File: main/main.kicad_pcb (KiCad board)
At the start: 2 copper layers, 39.2 x 36.2 mm, 90 parts, among them IC1 STM32U073CCU6, IC2 IC_TEXAS_TPS62743YFPR, IC3 IC_TEXAS_TPS62743YFPR, IC4 PAM8302AASCR, J3 USB_C_Receptacle_USB2.0_16P, J4 SM03B-SRSS-TB, Q1 DMG1012T-7, SW1 PTS810 SJK 250 SMTR LFS, U1 RP2350_60QFN, U2 IC_ESPIF_ESP32-C3-MINI-1-N4, U3 W25Q32RVXHJQ TR, U4 TMF8806, U6 450mA 4.2V, X1 XTAL_ABRACON_ABS07-32.768KHZ-T, Y1 ECS-120-8-33-JGN-TR

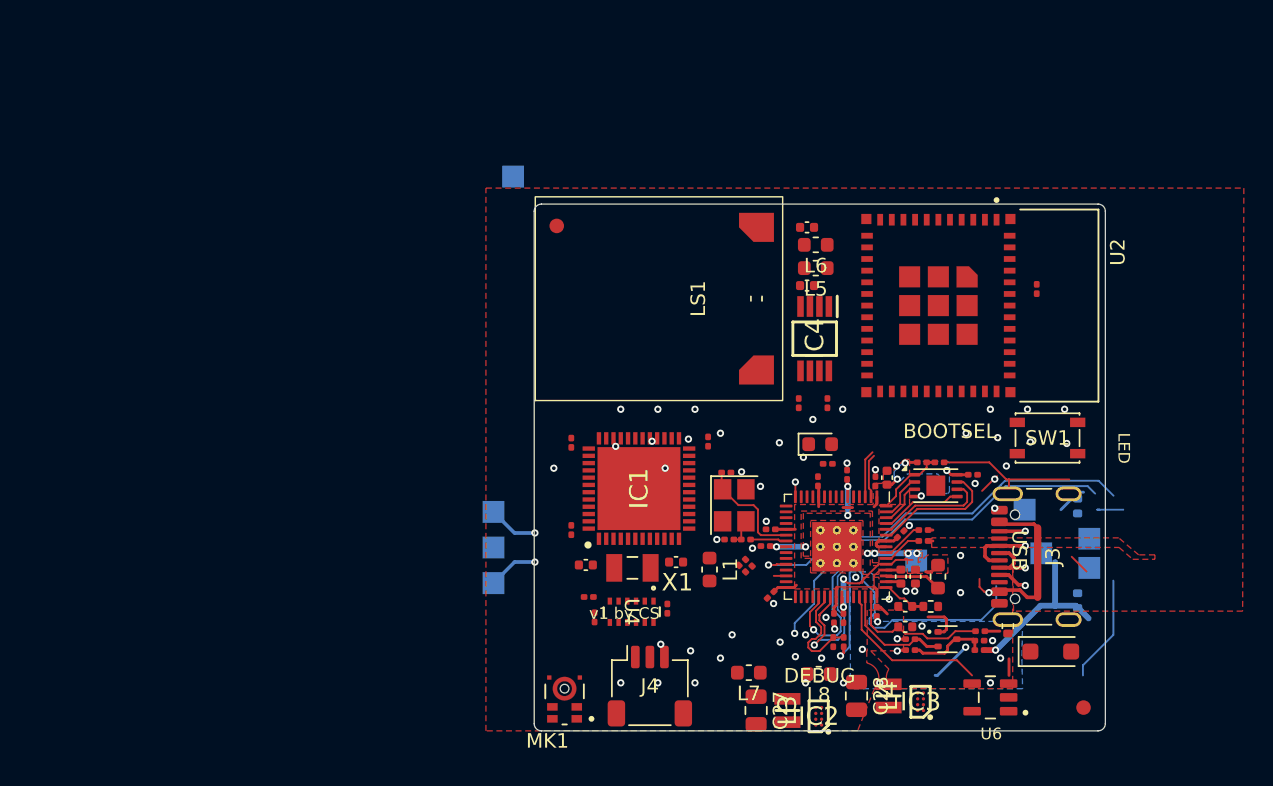
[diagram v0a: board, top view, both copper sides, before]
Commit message: last commit with pi-pico still on
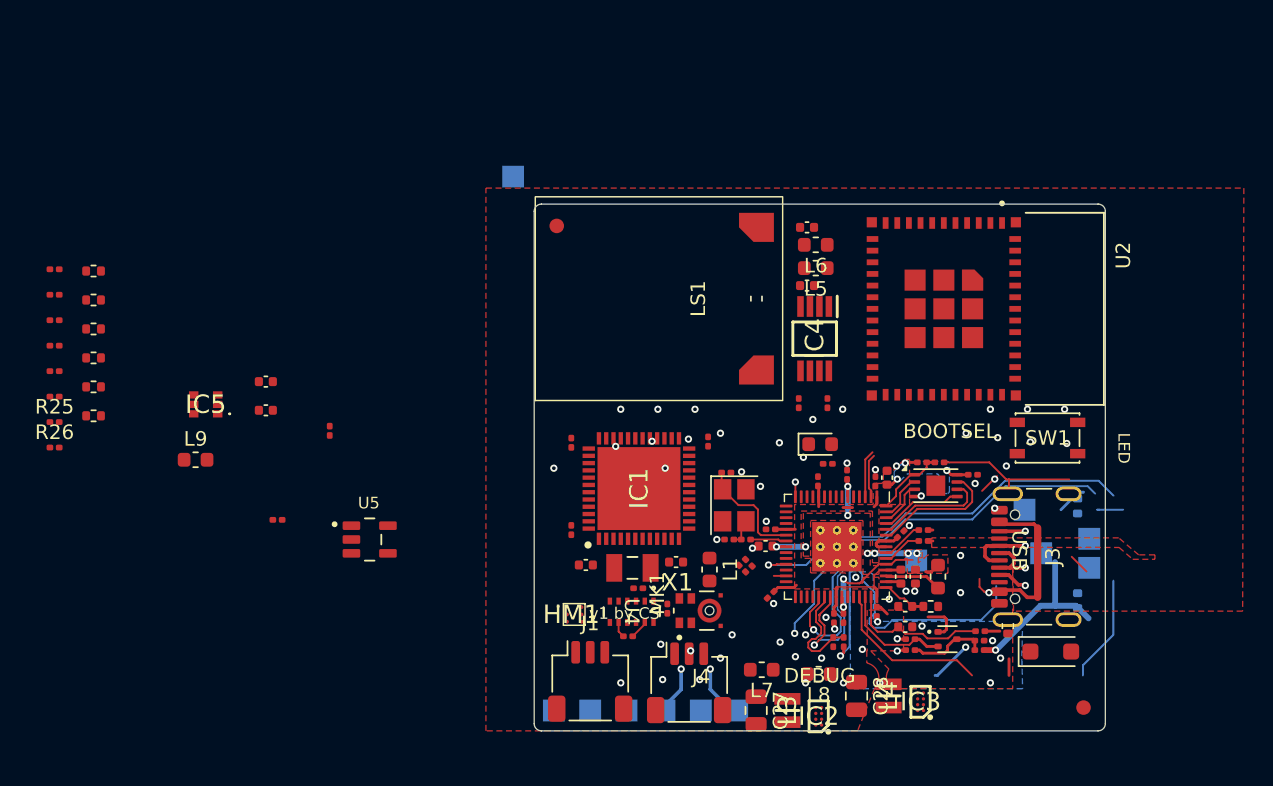
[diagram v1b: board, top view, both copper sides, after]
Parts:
- removed U6: 450mA 4.2V, smv_footprints:SOT95P280X145-5N
- added C35: 100NF_0201_10V_X7R, smv_footprints:C_0201_0603Metric, F.Cu at (111.6, 102.7)
- added C36: 100NF_0201_10V_X7R, smv_footprints:C_0201_0603Metric, F.Cu at (96.3, 85.5)
- added C37: 100NF_0201_10V_X7R, smv_footprints:C_0201_0603Metric, F.Cu at (96.3, 87.2)
- added C38: 100NF_0201_10V_X7R, smv_footprints:C_0201_0603Metric, F.Cu at (96.3, 89.0)
- added C39: 100NF_0201_10V_X7R, smv_footprints:C_0201_0603Metric, F.Cu at (96.3, 90.7)
- added C40: 100NF_0201_10V_X7R, smv_footprints:C_0201_0603Metric, F.Cu at (96.3, 92.5)
- added C41: 100NF_0201_10V_X7R, smv_footprints:C_0201_0603Metric, F.Cu at (96.3, 94.2)
- added C42: 4.7UF 0402 10V X7R, smv_footprints:C_0402_1005Metric, F.Cu at (110.8, 93.2)
- added C43: 4.7UF 0402 10V X7R, smv_footprints:C_0402_1005Metric, F.Cu at (110.8, 95.2)
- added HM1: HDC2010YPAR, smv_footprints:IC_TEXAS_HDC2010YPAR, F.Cu at (132.0, 109.2)
- added IC5: DIOD_PHOTO_VISHAY_VEML6035, smv_footprints:DIOD_PHOTO_VISHAY_VEML6035, F.Cu at (106.7, 94.8)
- added J1: SM03B-SRSS-TB, Connector_JST:JST_SH_SM03B-SRSS-TB_1x03-1MP_P1.00mm_Horizontal, F.Cu at (133.1, 113.8)
- added L9: INDC_BEAD_BLM18AG601SN1D, Inductor_SMD:L_0603_1608Metric, F.Cu at (106.0, 98.6)
- added R15: 10K 0402, smv_footprints:R_0402_1005Metric, F.Cu at (99.0, 89.6)
- added R2: 10K 0402, smv_footprints:R_0402_1005Metric, F.Cu at (99.0, 85.6)
- added R22: 10K 0402, smv_footprints:R_0402_1005Metric, F.Cu at (99.0, 91.6)
- added R23: 10K 0402, smv_footprints:R_0402_1005Metric, F.Cu at (99.0, 93.6)
- added R24: 10K 0402, smv_footprints:R_0402_1005Metric, F.Cu at (99.0, 95.5)
- added R25: 100R, Resistor_SMD:R_0201_0603Metric, F.Cu at (96.3, 96.0)
- added R26: 100R, Resistor_SMD:R_0201_0603Metric, F.Cu at (96.3, 97.7)
- added R8: 10K 0402, smv_footprints:R_0402_1005Metric, F.Cu at (99.0, 87.6)
- added TP11: TestPoint, TestPoint:TestPoint_Pad_1.5x1.5mm, B.Cu at (133.1, 115.8)
- added TP12: TestPoint, TestPoint:TestPoint_Pad_1.5x1.5mm, B.Cu at (135.6, 115.8)
- added TP4: TestPoint, TestPoint:TestPoint_Pad_1.5x1.5mm, B.Cu at (130.6, 115.8)
- added U5: 450mA 4.2V, smv_footprints:SOT95P280X145-5N, F.Cu at (117.9, 104.0)
- C13, C18, C19, C20, C21: value 4u7 -> 4.7UF 0402 10V X7R; footprint Capacitor_SMD:C_0402_1005Metric -> smv_footprints:C_0402_1005Metric
- C9: value 4u7 -> 4.7UF 0402 10V X7R; footprint Capacitor_SMD:C_0201_0603Metric -> smv_footprints:C_0402_1005Metric
- moved C32 49.6 mm to (115.2, 96.6)
- moved TP10 18.9 mm to (143.2, 115.8), turned to -90 degrees
- moved TP9 18.1 mm to (140.7, 115.8), turned to -90 degrees
- moved TP8 18.0 mm to (138.2, 115.8), turned to -90 degrees
- moved MK1 11.1 mm to (140.6, 108.9), turned to 90 degrees
- moved C33 3.45 mm to (136.4, 107.4), turned to 0 degrees
- moved J4 2.71 mm to (139.9, 113.9)
- moved C34 2.64 mm to (135.7, 110.7), turned to 0 degrees
- moved L7 0.91 mm to (144.9, 113.0)
- moved U2 0.44 mm to (160.1, 88.2)
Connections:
- net Net-(IC1-PA4) renamed /Low Power/AUDIO_OUT
- C10 pad 2: unconnected-(C10-Pad2) -> GND
- C19 pad 1: +1V1 -> unconnected-(C19-Pad1)
- C19 pad 2: GND -> unconnected-(C19-Pad2)
- C20 pad 2: GND -> unconnected-(C20-Pad2)
- C26 pad 1: Net-(IC1-VDDUSB) -> +1V8
- C27 pad 1: Net-(IC2-VOS) -> +1V8
- C31 pad 1: Net-(U4-VDDC) -> +3V3
- C32 pad 1: unconnected-(C32-Pad1) -> +1V8
- C32 pad 2: unconnected-(C32-Pad2) -> GND
- C33 pad 1: Net-(U4-GND) -> +3V3
- C33 pad 2: Net-(U4-VDD) -> GND
- C34 pad 1: Net-(U4-VDDV) -> +3V3
- C34 pad 2: Net-(U4-GNDV) -> GND
- C6 pad 2: unconnected-(C6-Pad2) -> GND
- C9 pad 2: GND -> unconnected-(C9-Pad2)
- IC1 pad 1: unconnected-(IC1-VBAT-Pad1) -> +1V8
- IC1 pad 19: unconnected-(IC1-PB1-Pad19) -> Net-(IC1-PB1)
- IC1 pad 23: unconnected-(IC1-VSS_1-Pad23) -> GND
- IC1 pad 25: unconnected-(IC1-PB12-Pad25) -> /Low Power/3V3_EN
- IC1 pad 26: unconnected-(IC1-PB13-Pad26) -> Net-(IC1-PB13)
- IC1 pad 27: unconnected-(IC1-PB14-Pad27) -> Net-(IC1-PB14)
- IC1 pad 28: unconnected-(IC1-PB15-Pad28) -> Net-(HM1-DRDY_/_INT)
- IC1 pad 34: unconnected-(IC1-PA13-Pad34) -> SD_ST
- IC1 pad 35: unconnected-(IC1-VSS_2-Pad35) -> GND
- IC1 pad 36: Net-(IC1-VDDUSB) -> +1V8
- IC1 pad 37: unconnected-(IC1-PA14-Pad37) -> SC_ST
- IC1 pad 38: unconnected-(IC1-PA15-Pad38) -> Net-(IC1-PA15)
- IC1 pad 39: unconnected-(IC1-PB3-Pad39) -> /Low Power/1V8_PP1
- IC1 pad 40: unconnected-(IC1-PB4-Pad40) -> /Low Power/1V8_PP2
- IC1 pad 41: unconnected-(IC1-PB5-Pad41) -> Net-(IC1-PB5)
- IC1 pad 42: unconnected-(IC1-PB6-Pad42) -> Net-(IC1-PB6)
- IC1 pad 43: unconnected-(IC1-PB7-Pad43) -> Net-(IC1-PB7)
- IC1 pad 45: unconnected-(IC1-PB8-Pad45) -> /Low Power/LIDAR_SCL
- IC1 pad 46: unconnected-(IC1-PB9-Pad46) -> /Low Power/LIDAR_SDA
- IC1 pad 47: unconnected-(IC1-VSS_3-Pad47) -> GND
- IC1 pad 49: unconnected-(IC1-EP-Pad49) -> GND
- IC2 pad A2: unconnected-(IC2-VIN-PadA2) -> Net-(IC2-EN)
- IC2 pad B1: unconnected-(IC2-EN-PadB1) -> Net-(IC2-EN)
- IC2 pad C1: unconnected-(IC2-VSEL1-PadC1) -> GND
- IC2 pad C2: Net-(IC2-VOS) -> +1V8
- IC2 pad D1: unconnected-(IC2-VSEL2-PadD1) -> Net-(IC2-EN)
- IC2 pad D2: unconnected-(IC2-VSEL3-PadD2) -> GND
- IC3 pad A2: unconnected-(IC3-VIN-PadA2) -> Net-(IC3-VIN)
- IC3 pad B1: unconnected-(IC3-EN-PadB1) -> /Low Power/3V3_EN
- IC3 pad C1: unconnected-(IC3-VSEL1-PadC1) -> Net-(IC3-VIN)
- IC3 pad D1: unconnected-(IC3-VSEL2-PadD1) -> Net-(IC3-VIN)
- IC3 pad D2: unconnected-(IC3-VSEL3-PadD2) -> Net-(IC3-VIN)
- IC4 pad 1: unconnected-(IC4-~{SD}-Pad1) -> Net-(IC1-PB1)
- IC4 pad 6: unconnected-(IC4-VDD-Pad6) -> +BATT
- L1 pad 1: unconnected-(L1-Pad1) -> +1V8
- L3 pad 2: Net-(IC2-VOS) -> +1V8
- L7 pad 1: Net-(IC2-VOS) -> +BATT
- L7 pad 2: unconnected-(L7-Pad2) -> Net-(IC2-EN)
- L8 pad 2: unconnected-(L8-Pad2) -> +3V3
- MK1 pad 1: unconnected-(MK1-DATA-Pad1) -> Net-(IC1-PB14)
- MK1 pad 2: unconnected-(MK1-SELECT-Pad2) -> GND
- MK1 pad 3_1: unconnected-(MK1-GND-Pad3_1) -> GND
- MK1 pad 3_2: unconnected-(MK1-GND__1-Pad3_2) -> GND
- MK1 pad 6: unconnected-(MK1-CLK-Pad6) -> Net-(IC1-PB13)
- MK1 pad 7: unconnected-(MK1-VDD-Pad7) -> +1V8
- U2 pad 1: Net-(U2-GND-Pad1) -> GND
- U2 pad 11: Net-(U2-GND-Pad1) -> GND
- U2 pad 14: Net-(U2-GND-Pad1) -> GND
- U2 pad 2: Net-(U2-GND-Pad1) -> GND
- U2 pad 3: unconnected-(U2-3V3-Pad3) -> +3V3
- U2 pad 36: Net-(U2-GND-Pad1) -> GND
- U2 pad 37: Net-(U2-GND-Pad1) -> GND
- U2 pad 38: Net-(U2-GND-Pad1) -> GND
- U2 pad 39: Net-(U2-GND-Pad1) -> GND
- U2 pad 40: Net-(U2-GND-Pad1) -> GND
- U2 pad 41: Net-(U2-GND-Pad1) -> GND
- U2 pad 42: Net-(U2-GND-Pad1) -> GND
- U2 pad 43: Net-(U2-GND-Pad1) -> GND
- U2 pad 44: Net-(U2-GND-Pad1) -> GND
- U2 pad 45: Net-(U2-GND-Pad1) -> GND
- U2 pad 46: Net-(U2-GND-Pad1) -> GND
- U2 pad 47: Net-(U2-GND-Pad1) -> GND
- U2 pad 48: Net-(U2-GND-Pad1) -> GND
- U2 pad 49_1: Net-(U2-GND-Pad1) -> GND
- U2 pad 49_2: Net-(U2-GND-Pad1) -> GND
- U2 pad 49_3: Net-(U2-GND-Pad1) -> GND
- U2 pad 49_4: Net-(U2-GND-Pad1) -> GND
- U2 pad 49_5: Net-(U2-GND-Pad1) -> GND
- U2 pad 49_6: Net-(U2-GND-Pad1) -> GND
- U2 pad 49_7: Net-(U2-GND-Pad1) -> GND
- U2 pad 49_8: Net-(U2-GND-Pad1) -> GND
- U2 pad 49_9: Net-(U2-GND-Pad1) -> GND
- U2 pad 50: Net-(U2-GND-Pad1) -> GND
- U2 pad 51: Net-(U2-GND-Pad1) -> GND
- U2 pad 52: Net-(U2-GND-Pad1) -> GND
- U2 pad 53: Net-(U2-GND-Pad1) -> GND
- U4 pad 1: Net-(U4-VDDC) -> +3V3
- U4 pad 11: Net-(U4-GNDV) -> GND
- U4 pad 12: Net-(U4-VDDV) -> +3V3
- U4 pad 3: unconnected-(U4-GPIO0-Pad3) -> /Low Power/1V8_PP1
- U4 pad 4: unconnected-(U4-INT-Pad4) -> Net-(IC1-PA15)
- U4 pad 5: unconnected-(U4-SCL-Pad5) -> /Low Power/LIDAR_SCL
- U4 pad 6: unconnected-(U4-SDA-Pad6) -> /Low Power/LIDAR_SDA
- U4 pad 7: Net-(U4-VDD) -> GND
- U4 pad 8: Net-(U4-GND) -> +3V3
- U4 pad 9: unconnected-(U4-EN-Pad9) -> /Low Power/1V8_PP1
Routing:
- net GND: track 14.6 -> 16.3 mm, vias 49 -> 48
- net +3V3: track 23.5 -> 24.6 mm, vias 3 -> 4
- net unconnected-(C6-Pad2): track 0.38 -> 0.00 mm, vias 1 -> 0
- net unconnected-(U6-VBAT-Pad3): vias 1 -> 0
- net unconnected-(L8-Pad2): vias 1 -> 0
- net unconnected-(IC4-~{SD}-Pad1): vias 1 -> 0
- net unconnected-(IC1-PA8-Pad29): vias 0 -> 1
- net unconnected-(IC1-EP-Pad49): vias 1 -> 0
- net unconnected-(C9-Pad2): vias 0 -> 1
- net unconnected-(C19-Pad2): vias 0 -> 1
- net Net-(U2-GND-Pad1): vias 3 -> 0
- net Net-(IC1-PB1): vias 0 -> 1
- net (no net): vias 0 -> 4
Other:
- board text added: "PICO SWD GND SWC"
- board text added: "STM SWD GND SWC"
- board text removed: "CLK"
- board text removed: "DIO"
- board text removed: "GND"

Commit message: added leds and removed pico, changed outline
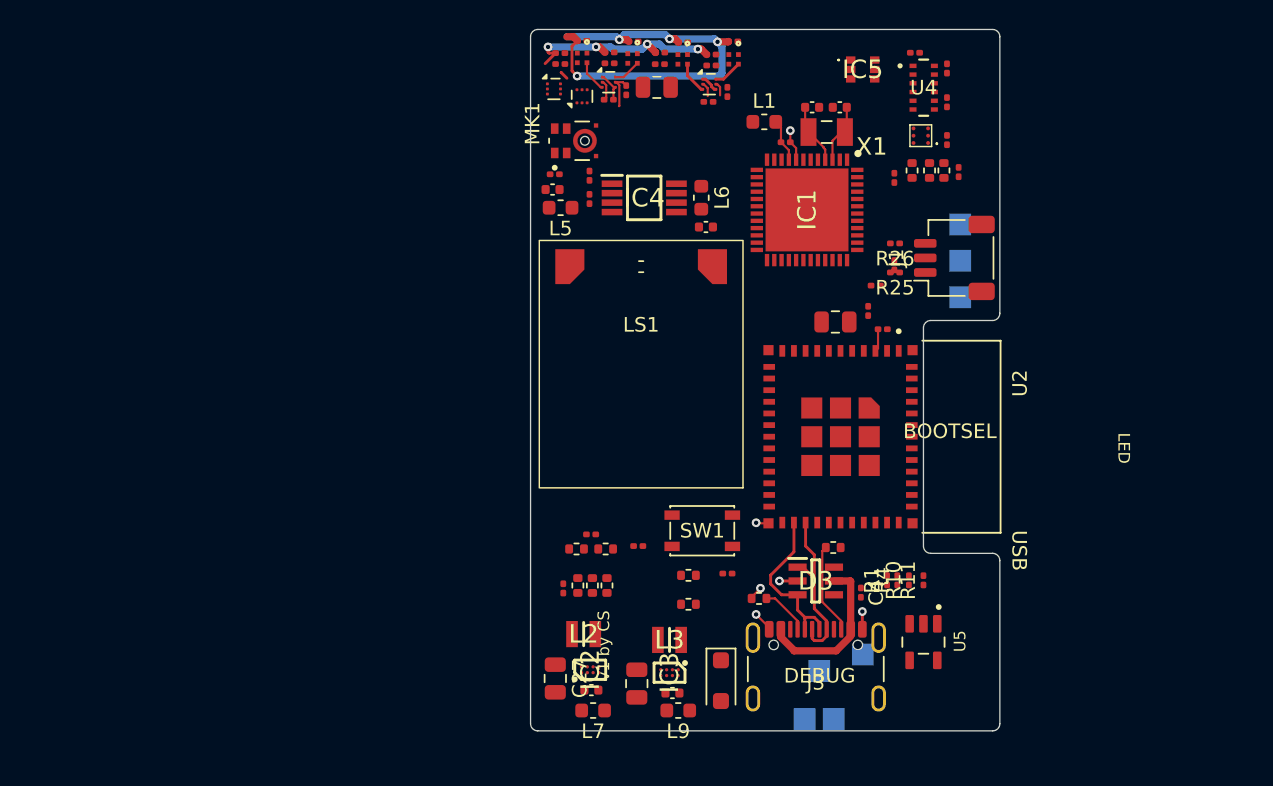
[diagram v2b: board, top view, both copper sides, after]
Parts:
- removed C10, C11, C12, C14, C15: 100NF_0201_10V_X7R, smv_footprints:C_0201_0603Metric
- removed C13, C18, C19, C20, C21, C9: 4.7UF 0402 10V X7R, smv_footprints:C_0402_1005Metric
- removed C16, C17: 15p, Capacitor_SMD:C_0201_0603Metric
- removed C28: 10UF_0805_16V_X7R, smv_footprints:C_0805_2012Metric
- removed D2: LTST-C191KGKT, LED_SMD:LED_0603_1608Metric
- removed FID1, FID2: Fiducial, Fiducial:Fiducial_1mm_Mask2mm
- removed J4: SM03B-SRSS-TB, Connector_JST:JST_SH_SM03B-SRSS-TB_1x03-1MP_P1.00mm_Horizontal
- removed L4: 2.2u, smv_footprints:IND_MURATA_DFE201610P-2R2M=P2
- removed L8: INDC_BEAD_BLM18AG601SN1D, Inductor_SMD:L_0603_1608Metric
- removed R17: 33R, Resistor_SMD:R_0402_1005Metric
- removed R18: 100R, Resistor_SMD:R_0201_0603Metric
- removed R3: 470R, Resistor_SMD:R_0201_0603Metric
- removed TP10, TP5, TP7, TP8, TP9: TestPoint, TestPoint:TestPoint_Pad_1.5x1.5mm
- removed U1: RP2350_60QFN, Pico 2 C:RP2350-QFN-60-1EP_7x7_P0.4mm_EP3.4x3.4mm_ThermalVias
- removed U3: W25Q32RVXHJQ TR, Package_DFN_QFN:TDFN-8-1EP_3x2mm_P0.5mm_EP1.3x1.4mm
- removed Y1: ECS-120-8-33-JGN-TR, Crystal:Crystal_SMD_SeikoEpson_FA238-4Pin_3.2x2.5mm
- added D3: PRTR5V0U4D,125, smv_footprints:SOT95P275X110-6N, F.Cu at (148.6, 106.9)
- added LED1: RGB, smv_footprints:DIOD_CREE_UHD111A-FKA-C3K23E1L3VG5ZB3Z3, F.Cu at (136.0, 71.0)
- added LED2: RGB, smv_footprints:DIOD_CREE_UHD111A-FKA-C3K23E1L3VG5ZB3Z3, F.Cu at (132.5, 71.0)
- added LED3: RGB, smv_footprints:DIOD_CREE_UHD111A-FKA-C3K23E1L3VG5ZB3Z3, F.Cu at (143.0, 71.1)
- added LED4: RGB, smv_footprints:DIOD_CREE_UHD111A-FKA-C3K23E1L3VG5ZB3Z3, F.Cu at (139.5, 71.1)
- added Q2: TRAN_DIODES_DMN2991UDJ_7A, Package_TO_SOT_SMD:SOT-963, F.Cu at (132.5, 73.6)
- added Q3: TRAN_DIODES_DMP22D5UDJ-7, Package_TO_SOT_SMD:SOT-963, F.Cu at (134.4, 72.6)
- added Q4: TRAN_DIODES_DMP22D5UDJ-7, Package_TO_SOT_SMD:SOT-963, F.Cu at (141.3, 72.8)
- added R27: 150, Resistor_SMD:R_0201_0603Metric, F.Cu at (137.9, 70.6)
- added R28: 150, Resistor_SMD:R_0201_0603Metric, F.Cu at (142.9, 69.8)
- added R29: 150, Resistor_SMD:R_0201_0603Metric, F.Cu at (141.4, 70.7)
- added R30: 150, Resistor_SMD:R_0201_0603Metric, F.Cu at (132.5, 69.8)
- added R31: 150, Resistor_SMD:R_0201_0603Metric, F.Cu at (131.0, 70.6)
- added R32: 150, Resistor_SMD:R_0201_0603Metric, F.Cu at (136.1, 69.8)
- added R33: 150, Resistor_SMD:R_0201_0603Metric, F.Cu at (134.4, 70.6)
- added R34: 10k, Resistor_SMD:R_0201_0603Metric, F.Cu at (134.4, 73.8)
- added R35: 10k, Resistor_SMD:R_0201_0603Metric, F.Cu at (135.6, 73.2)
- added R36: 10k, Resistor_SMD:R_0201_0603Metric, F.Cu at (141.2, 74.0)
- added R37: 10k, Resistor_SMD:R_0201_0603Metric, F.Cu at (142.5, 73.3)
- C3: value 1n -> 100NF_0201_10V_X7R; footprint Capacitor_SMD:C_0201_0603Metric -> smv_footprints:C_0201_0603Metric
- C4: value 100NF_0201_10V_X7R -> 1n; footprint smv_footprints:C_0201_0603Metric -> Capacitor_SMD:C_0201_0603Metric
- C6, C7, C8: value 100NF_0201_10V_X7R -> 10UF_0805_16V_X7R; footprint smv_footprints:C_0201_0603Metric -> smv_footprints:C_0805_2012Metric
- L2: value 3u3 -> 2.2u; footprint Inductor_SMD:L_0603_1608Metric -> smv_footprints:IND_MURATA_DFE201610P-2R2M=P2
- Q1: value DMG1012T-7 -> TRAN_DIODES_DMN2991UDJ_7A; footprint Package_TO_SOT_SMD:SOT-523 -> Package_TO_SOT_SMD:SOT-963
- R12, R13: value 27R -> 150
- R14: value 1k -> 150
- R16: value 100k -> 150
- R19: value 100R -> 150
- R20, R21: moved to F.Cu
- R5: value 100k -> 1.2M 0402; footprint Resistor_SMD:R_0201_0603Metric -> smv_footprints:R_0402_1005Metric
- R6: value 100k -> 680K 0402; footprint Resistor_SMD:R_0201_0603Metric -> smv_footprints:R_0402_1005Metric
- R7: value 200R -> 1.2M 0402; footprint Resistor_SMD:R_0402_1005Metric -> smv_footprints:R_0402_1005Metric
- R9: value 1R -> 680K 0402; footprint Resistor_SMD:R_0201_0603Metric -> smv_footprints:R_0402_1005Metric
- moved C39 62.9 mm to (157.6, 76.6), turned to 90 degrees
- moved C36 62.5 mm to (158.4, 78.8), turned to 90 degrees
- moved R26 59.4 mm to (154.0, 83.7), turned to 180 degrees
- moved R2 58.8 mm to (157.4, 78.7), turned to -90 degrees
- moved R25 58.7 mm to (154.0, 85.7), turned to 180 degrees
- moved R8 58.1 mm to (156.4, 78.7), turned to -90 degrees
- moved R15 57.3 mm to (155.2, 78.7), turned to -90 degrees
- moved C38 56.5 mm to (152.7, 86.6), turned to 180 degrees
- moved C37 51.3 mm to (146.5, 76.8)
- moved IC5 50.7 mm to (151.8, 71.8), turned to 180 degrees
- moved Q1 46.5 mm to (130.6, 73.1)
- moved C34 44.7 mm to (155.4, 70.6), turned to 180 degrees
- moved R16 44.6 mm to (134.4, 71.3)
- moved C35 43.6 mm to (153.2, 89.6)
- moved C40 41.9 mm to (136.4, 104.5), turned to 180 degrees
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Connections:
- net /Low Power/1V8_PP1 renamed /Sensors and STM32/1V8_PP1
- net /Low Power/1V8_PP2 renamed Net-(IC1-PB4)
- net /Low Power/AUDIO_OUT renamed /Sensors and STM32/AUDIO_OUT
- net /Low Power/LIDAR_SCL renamed /Sensors and STM32/LIDAR_SCL
- net /Low Power/LIDAR_SDA renamed /Sensors and STM32/LIDAR_SDA
- net QSPI_SS renamed Net-(R11-Pad2)
- C3 pad 1: Net-(Q1-D) -> VBUS_SENSE
- C4 pad 1: +3V3 -> VBUS
- C5 pad 1: +3V3 -> VBAT_SENSE
- D1 pad 1: unconnected-(D1-K-Pad1) -> Net-(D1-K)
- IC1 pad 25: /Low Power/3V3_EN -> /Sensors and STM32/3V3_EN
- IC3 pad B1: /Low Power/3V3_EN -> /3V3_EN
- IC3 pad C2: Net-(IC3-VOS) -> +3V3
- L2 pad 1: +1V1 -> Net-(IC2-SW)
- L2 pad 2: Net-(U1-VREG_LX) -> +1V8
- L3 pad 1: Net-(IC2-SW) -> Net-(IC3-SW)
- L3 pad 2: +1V8 -> +3V3
- Q1 pad 1: +3V3 -> GND
- Q1 pad 2: GPIO29_ADC3 -> LEDB
- Q1 pad 3: Net-(Q1-D) -> Net-(Q1B-DRAIN)
- R12 pad 1: USB_DP -> Net-(LED3-Pad3)
- R12 pad 2: Net-(U1-USB_DP) -> Net-(Q2B-DRAIN)
- R13 pad 1: USB_DM -> Net-(LED2-Pad3)
- R13 pad 2: Net-(U1-USB_DM) -> Net-(Q2B-DRAIN)
- R14 pad 1: XOUT -> Net-(LED4-Pad3)
- R14 pad 2: Net-(C17-Pad1) -> Net-(Q2B-DRAIN)
- R16 pad 1: GPIO29_ADC3 -> Net-(LED1-Pad3)
- R16 pad 2: GND -> Net-(Q2B-DRAIN)
- R19 pad 1: SC -> Net-(LED4-Pad1)
- R19 pad 2: SWCLK -> Net-(Q1A-DRAIN)
- R5 pad 1: VS -> VBUS_SENSE
- R5 pad 2: Net-(Q1-D) -> VBUS
- R6 pad 1: Net-(Q1-D) -> GND
- R6 pad 2: GND -> VBUS_SENSE
- R7 pad 1: +3V3 -> VBAT_SENSE
- R7 pad 2: ADC_VREF -> +BATT
- R9 pad 1: ADC_VREF -> GND
- R9 pad 2: Net-(U1-ADC_AVDD) -> VBAT_SENSE
- U2 pad 12: unconnected-(U2-IO0-Pad12) -> LED1
- U2 pad 13: unconnected-(U2-IO1-Pad13) -> LED2
- U2 pad 18: unconnected-(U2-IO4-Pad18) -> LEDB
- U2 pad 19: unconnected-(U2-IO5-Pad19) -> LEDR
- U2 pad 20: unconnected-(U2-IO6-Pad20) -> LEDG
- U2 pad 26: unconnected-(U2-IO18-Pad26) -> USB_DM
- U2 pad 27: unconnected-(U2-IO19-Pad27) -> USB_DP
- U2 pad 5: unconnected-(U2-IO2-Pad5) -> LED3
- U2 pad 6: unconnected-(U2-IO3-Pad6) -> LED4
- U5 pad 2: unconnected-(U5-VSS-Pad2) -> GND
- U5 pad 4: unconnected-(U5-VDD-Pad4) -> Net-(D1-K)
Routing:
- net GPIO23: track 34.1 -> 0.00 mm, vias 1 -> 0
- net GPIO25: track 32.0 -> 0.00 mm, vias 1 -> 0
- net Net-(Q1A-DRAIN): track 0.00 -> 29.4 mm, vias 0 -> 4
- net VBUS: track 36.4 -> 11.7 mm, vias 2 -> 0
- net +3V3: track 24.6 -> 4.90 mm, vias 4 -> 0
- net +1V1: track 19.6 -> 0.00 mm, vias 10 -> 0
- net Net-(Q1B-DRAIN): track 0.00 -> 14.9 mm, vias 0 -> 4
- net Net-(SW1-A): track 13.1 -> 0.00 mm, vias 2 -> 0
- net VS: track 11.8 -> 0.00 mm, vias 1 -> 0
- net RUN: track 11.8 -> 0.00 mm, vias 2 -> 0
- net GPIO28_ADC2: track 11.2 -> 0.00 mm
- net Net-(U1-ADC_AVDD): track 9.99 -> 0.00 mm
- net QSPI_SD3: track 8.91 -> 0.00 mm
- net GND: track 16.3 -> 7.95 mm, vias 48 -> 6
- net GPIO29_ADC3: track 7.89 -> 0.00 mm
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- removed copper zone on F.Cu, net +1V1
- removed copper zone on B.Cu, net +3V3
- removed copper zone on F.Cu, net +3V3
- removed copper zone on B.Cu, net GND
- removed copper zone on F.Cu, net GND
- removed copper zone on F.Cu, net USB_DM
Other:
- board size 39.2 x 36.2 mm -> 32.2 x 48.2 mm
- board text removed: "PICO SWD GND SWC"
